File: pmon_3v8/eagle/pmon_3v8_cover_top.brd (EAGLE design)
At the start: 66 x 66 mm, 4 parts, among them J1 USB, J2 USB

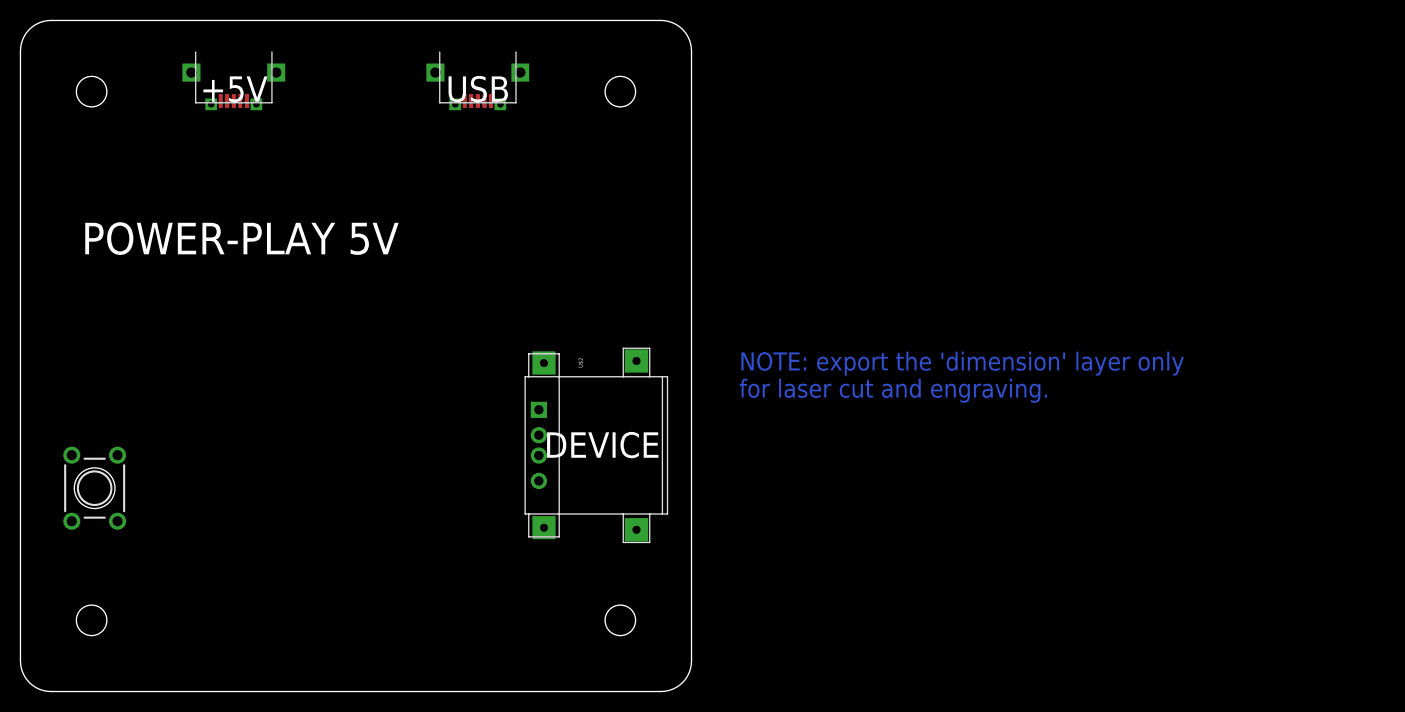
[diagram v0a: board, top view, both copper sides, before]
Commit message: Cleaned up laser cut files.
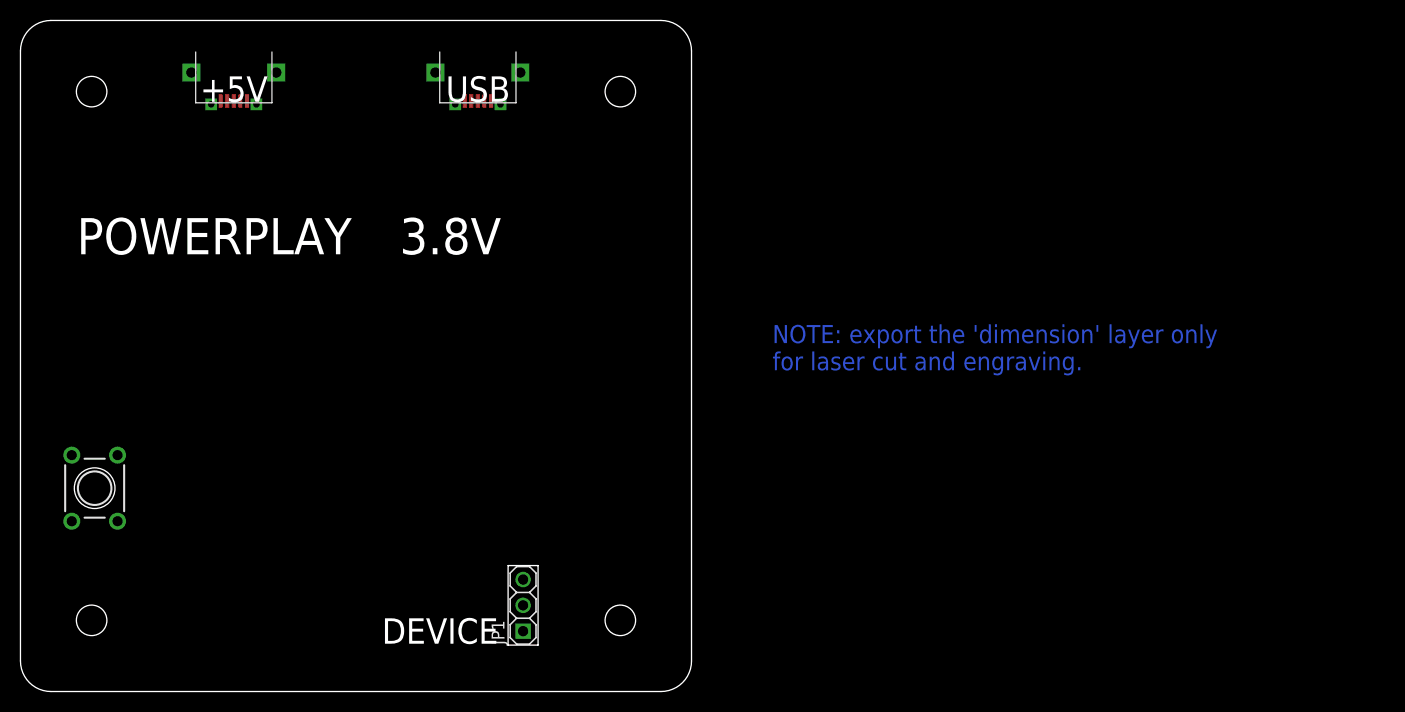
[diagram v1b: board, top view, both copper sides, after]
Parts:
- removed U$2: USB_A, pmon_5v:USB_A
- added JP1: (no value), pmon_oled:1X03
- J1, J2: device pmon_5v:USB-MICRO-ZX62RD-AB-5P8 -> pmon_3v8:USB-MICRO-ZX62RD-AB-5P8
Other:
- outline, holes or cut-outs redrawn
- board text added: "3.8V"
- board text added: "POWERPLAY"
- board text removed: "POWER-PLAY 5V"
